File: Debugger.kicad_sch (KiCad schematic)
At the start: 22 parts, among them J1 Header internal clock, J2 I/O, Q1 BC546, SW1 Single step, U1 NE555P, U2 74LS00, U3 74LS74

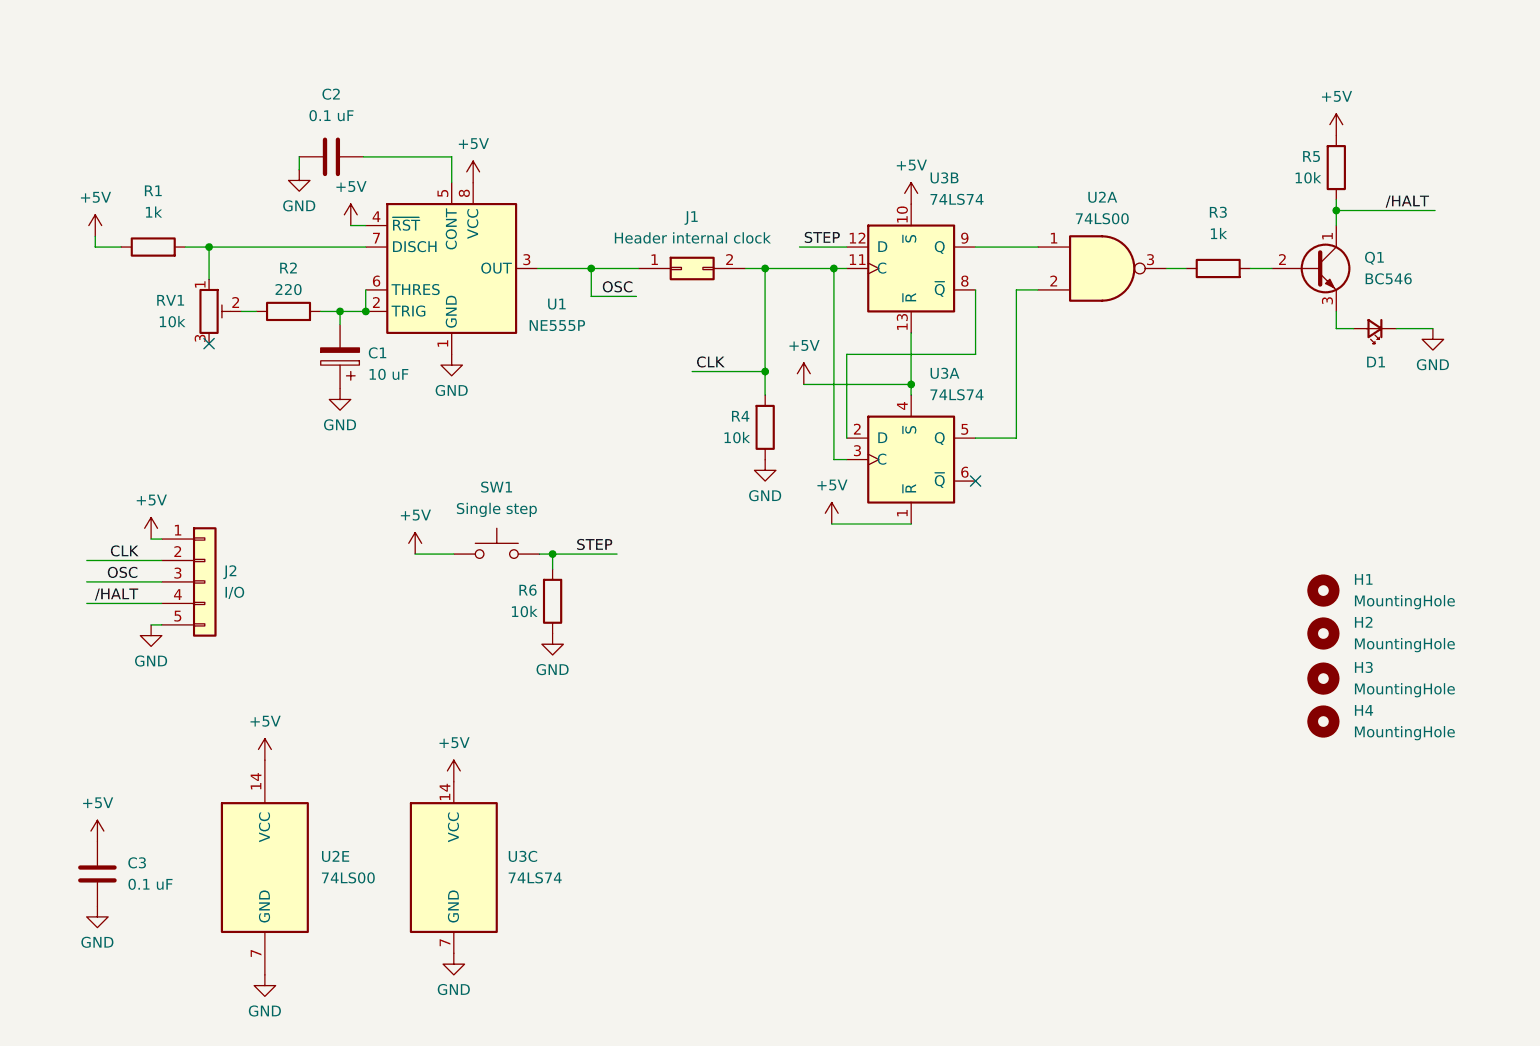
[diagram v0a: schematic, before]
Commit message: Schematic: schmitt trigger, auxilary ports
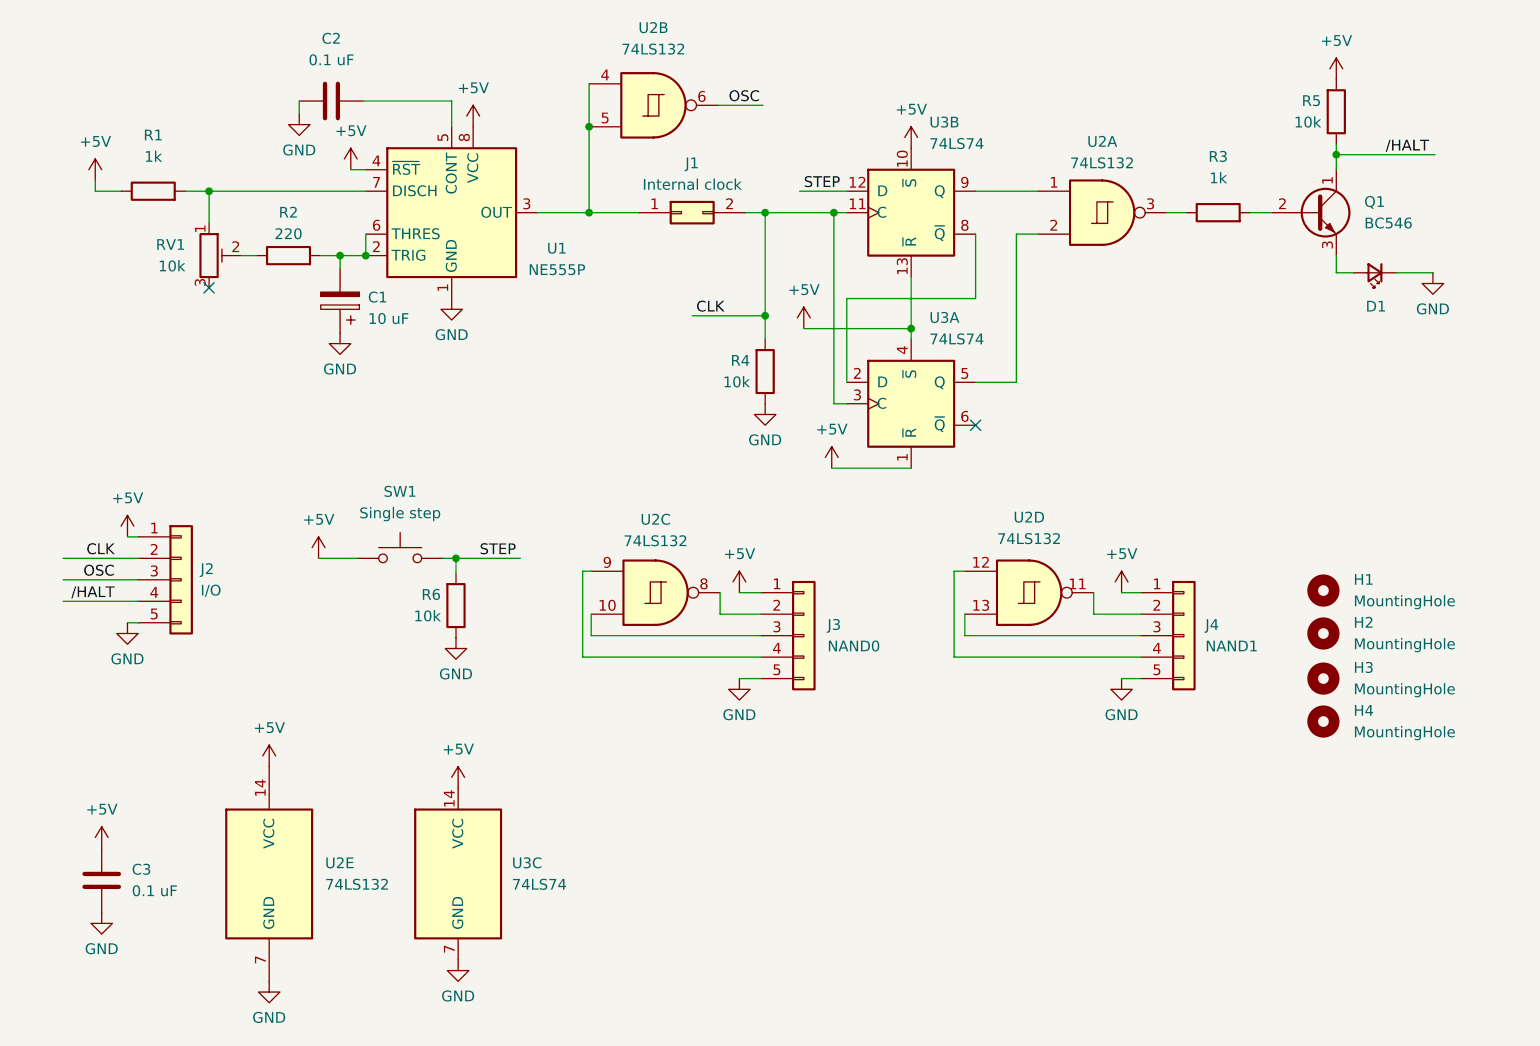
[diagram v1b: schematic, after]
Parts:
- removed U2: 74LS00, Package_DIP:DIP-14_W10.16mm, symbol 74xx:74LS00
- added J3: NAND0, Connector_PinHeader_1.00mm:PinHeader_1x05_P1.00mm_Vertical, symbol Connector_Generic:Conn_01x05
- added J4: NAND1, Connector_PinHeader_1.00mm:PinHeader_1x05_P1.00mm_Vertical, symbol Connector_Generic:Conn_01x05
- added U2: 74LS132, Package_DIP:DIP-14_W7.62mm_Socket, symbol 74xx:74LS132
- added unit 2 of U3
- added unit 3 of U3
- J1: value Header internal clock -> Internal clock
- U1: footprint Package_DIP:DIP-8_W7.62mm -> Package_DIP:DIP-8_W7.62mm_Socket
- U3: footprint Package_DIP:DIP-14_W10.16mm -> Package_DIP:DIP-14_W7.62mm_Socket
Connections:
- net +5V: now also J3.1 (Pin_1), J4.1 (Pin_1), U2.14 (VCC), U3.10 (~{S}), U3.13 (~{R}), U3.14 (VCC); no longer U3.10 (~{S}), U3.13 (~{R}), U3.14 (VCC)
- net CLK: now also U3.11 (C); no longer U3.11 (C)
- net GND: now also J3.5 (Pin_5), J4.5 (Pin_5), U2.7 (GND), U3.7 (GND); no longer U3.7 (GND)
- net OSC: now also U2.6; no longer J1.1 (Pin_1), U1.3 (OUT)
- net STEP: now also U3.12 (D); no longer U3.12 (D)
- net at U3.2 (D): now also U3.8 (~{Q}); no longer U3.8 (~{Q})
- net at U3.5 (Q): now also U2.2
- net at R3.1: now also U2.3
- new net: U2.1, U3.9 (Q)
- new net: J3.3 (Pin_3), U2.10
- new net: J4.2 (Pin_2), U2.11
- new net: J4.4 (Pin_4), U2.12
- new net: J4.3 (Pin_3), U2.13
- new net: J1.1 (Pin_1), U1.3 (OUT), U2.4, U2.5
- new net: J3.2 (Pin_2), U2.8
- new net: J3.4 (Pin_4), U2.9
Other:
- moved on the sheet: C1, C2, C3, D1, J1, J2, Q1, R1, R2, R3, R4, R5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

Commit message: Schematic: fix power flag
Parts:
- added unit 3 of U2
- added unit 5 of U2
- added unit 4 of U2
- added unit 1 of U2
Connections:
- net +5V: now also U2.14 (VCC); no longer U2.14 (VCC)
- net GND: now also U2.7 (GND); no longer U2.7 (GND)
- net at U3.9 (Q): now also U2.1; no longer U2.1
- net at J3.3 (Pin_3): now also U2.10; no longer U2.10
- net at J4.2 (Pin_2): now also U2.11; no longer U2.11
- net at J4.4 (Pin_4): now also U2.12; no longer U2.12
- net at J4.3 (Pin_3): now also U2.13; no longer U2.13
- net at U3.5 (Q): now also U2.2; no longer U2.2
- net at R3.1: now also U2.3; no longer U2.3
- net at J3.2 (Pin_2): now also U2.8; no longer U2.8
- net at J3.4 (Pin_4): now also U2.9; no longer U2.9
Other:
- moved on the sheet: J2
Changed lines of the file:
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@@
 	)
 	(junction
+		(at 34.544 85.852)
+		(diameter 0)
+		(color 0 0 0 0)
+	)
+	(junction
+		(at 34.544 75.692)
+		(diameter 0)
+		(color 0 0 0 0)
+	)
+	(junction
 		(at 82.55 27.178)
 		(diameter 0)
@@
 	(wire
 		(pts
-			(xy 27.94 75.692) (xy 29.21 75.692)
+			(xy 34.544 75.692) (xy 35.814 75.692)
 		)
 		(stroke
@@
 	(wire
 		(pts
+			(xy 29.972 85.852) (xy 34.544 85.852)
+		)
+		(stroke
+			(width 0)
+			(type default)
+		)
+	)
+	(wire
+		(pts
 			(xy 125.73 89.916) (xy 147.828 89.916)
 		)
@@
 	(wire
 		(pts
+			(xy 29.972 75.692) (xy 34.544 75.692)
+		)
+		(stroke
+			(width 0)
+			(type default)
+		)
+	)
+	(wire
+		(pts
 			(xy 133.096 39.878) (xy 135.636 39.878)
 		)
@@
 	(wire
 		(pts
-			(xy 20.32 78.232) (xy 29.21 78.232)
+			(xy 26.924 78.232) (xy 35.814 78.232)
 		)
 		(stroke
@@
 	(wire
 		(pts
-			(xy 20.32 80.772) (xy 29.21 80.772)
+			(xy 26.924 80.772) (xy 35.814 80.772)
 		)
 		(stroke
@@
 	(wire
 		(pts
-			(xy 27.94 85.852) (xy 29.21 85.852)
+			(xy 34.544 85.852) (xy 35.814 85.852)
 		)
 		(stroke
@@
 	(wire
 		(pts
-			(xy 20.32 83.312) (xy 29.21 83.312)
+			(xy 26.924 83.312) (xy 35.814 83.312)
 		)
 		(stroke
@@
 	)
 	(label "OSC"
-		(at 26.416 80.772 180)
+		(at 33.02 80.772 180)
 		(effects
 			(font
@@
 	)
 	(label "{slash}HALT"
-		(at 26.416 83.312 180)
+		(at 33.02 83.312 180)
 		(effects
 			(font
@@
 	)
 	(label "CLK"
-		(at 26.416 78.232 180)
+		(at 33.02 78.232 180)
 		(effects
 			(font
@@
 	(symbol
 		(lib_id "power:GND")
-		(at 27.94 85.852 0)
+		(at 34.544 85.852 0)
 		(unit 1)
 		(body_style 1)
@@
 		(fields_autoplaced yes)
 		(property "Reference" "#PWR021"
-			(at 27.94 92.202 0)
+			(at 34.544 92.202 0)
 			(hide yes)
 			(show_name no)
@@
 		)
 		(property "Value" "GND"
-			(at 27.94 90.17 0)
+			(at 34.544 90.17 0)
 			(show_name no)
 			(do_not_autoplace no)
@@
 		)
 		(property "Footprint" ""
-			(at 27.94 85.852 0)
+			(at 34.544 85.852 0)
 			(hide yes)
 			(show_name no)
@@
 		)
 		(property "Datasheet" ""
-			(at 27.94 85.852 0)
+			(at 34.544 85.852 0)
 			(hide yes)
 			(show_name no)
@@
 		)
 		(property "Description" "Power symbol creates a global label with name \"GND\" , ground"
-			(at 27.94 85.852 0)
+			(at 34.544 85.852 0)
 			(hide yes)
 			(show_name no)
@@
 	(symbol
 		(lib_id "Connector_Generic:Conn_01x05")
-		(at 34.29 80.772 0)
+		(at 40.894 80.772 0)
 		(unit 1)
 		(body_style 1)
@@
 		(fields_autoplaced yes)
 		(property "Reference" "J2"
-			(at 36.576 79.5019 0)
+			(at 43.18 79.5019 0)
 			(show_name no)
 			(do_not_autoplace no)
@@
 		)
 		(property "Value" "I/O"
-			(at 36.576 82.0419 0)
+			(at 43.18 82.0419 0)
 			(show_name no)
 			(do_not_autoplace no)
@@
 		)
 		(property "Footprint" "Connector_PinHeader_1.00mm:PinHeader_1x05_P1.00mm_Vertical"
-			(at 34.29 80.772 0)
+			(at 40.894 80.772 0)
 			(hide yes)
 			(show_name no)
@@
 		)
 		(property "Datasheet" ""
-			(at 34.29 80.772 0)
+			(at 40.894 80.772 0)
 			(hide yes)
 			(show_name no)
@@
 		)
 		(property "Description" "Generic connector, single row, 01x05, script generated (kicad-library-utils/schlib/autogen/connector/)"
-			(at 34.29 80.772 0)
+			(at 40.894 80.772 0)
 			(hide yes)
 			(show_name no)
@@
 	(symbol
 		(lib_id "power:+5V")
-		(at 27.94 75.692 0)
+		(at 34.544 75.692 0)
 		(unit 1)
 		(body_style 1)
@@
 		(fields_autoplaced yes)
 		(property "Reference" "#PWR020"
-			(at 27.94 79.502 0)
+			(at 34.544 79.502 0)
 			(hide yes)
 			(show_name no)
@@
 		)
 		(property "Value" "+5V"
-			(at 27.94 71.12 0)
+			(at 34.544 71.12 0)
 			(show_name no)
 			(do_not_autoplace no)
@@
 		)
 		(property "Footprint" ""
-			(at 27.94 75.692 0)
+			(at 34.544 75.692 0)
 			(hide yes)
 			(show_name no)
@@
 		)
 		(property "Datasheet" ""
-			(at 27.94 75.692 0)
+			(at 34.544 75.692 0)
 			(hide yes)
 			(show_name no)
@@
 		)
 		(property "Description" "Power symbol creates a global label with name \"+5V\""
-			(at 27.94 75.692 0)
+			(at 34.544 75.692 0)
 			(hide yes)
 			(show_name no)
@@
 	)
 	(symbol
+		(lib_id "power:PWR_FLAG")
+		(at 29.972 85.852 90)
+		(unit 1)
+		(body_style 1)
+		(exclude_from_sim no)
+		(in_bom yes)
+		(on_board yes)
+		(in_pos_files yes)
+		(dnp no)
+		(fields_autoplaced yes)
+		(property "Reference" "#FLG01"
+			(at 28.067 85.852 0)
+			(hide yes)
+			(show_name no)
+			(do_not_autoplace no)
+			(effects
+				(font
+					(size 1.27 1.27)
+				)
+			)
+		)
+		(property "Value" "PWR_FLAG"
+			(at 26.162 85.8519 90)
+			(show_name no)
+			(do_not_autoplace no)
+			(effects
+				(font
+					(size 1.27 1.27)
+				)
+				(justify left)
+			)
+		)
+		(property "Footprint" ""
+			(at 29.972 85.852 0)
+			(hide yes)
+			(show_name no)
+			(do_not_autoplace no)
+			(effects
+				(font
+					(size 1.27 1.27)
+				)
+			)
+		)
+		(property "Datasheet" ""
+			(at 29.972 85.852 0)
+			(hide yes)
+			(show_name no)
+			(do_not_autoplace no)
+			(effects
+				(font
+					(size 1.27 1.27)
+				)
+			)
+		)
+		(property "Description" "Special symbol for telling ERC where power comes from"
+			(at 29.972 85.852 0)
+			(hide yes)
+			(show_name no)
+			(do_not_autoplace no)
+			(effects
+				(font
+					(size 1.27 1.27)
+				)
+			)
+		)
+		(pin "1"
+		)
+		(instances
+			(project "Debugger"
+				(path "/a8de7697-6937-4325-b328-e8937268e3c6"
+					(reference "#FLG01")
+					(unit 1)
+				)
+			)
+		)
+	)
+	(symbol
 		(lib_id "Transistor_BJT:BC546")
 		(at 168.402 37.338 0)
@@
 					(unit 1)
 				)
+			)
+		)
+	)
+	(symbol
+		(lib_id "power:PWR_FLAG")
+		(at 29.972 75.692 90)
+		(unit 1)
+		(body_style 1)
+		(exclude_from_sim no)
+		(in_bom yes)
+		(on_board yes)
+		(in_pos_files yes)
+		(dnp no)
+		(fields_autoplaced yes)
+		(property "Reference" "#FLG02"
+			(at 28.067 75.692 0)
+			(hide yes)
+			(show_name no)
+			(do_not_autoplace no)
+			(effects
+				(font
+					(size 1.27 1.27)
+				)
+			)
+		)
+		(property "Value" "PWR_FLAG"
+			(at 26.162 75.6919 90)
+			(show_name no)
+			(do_not_autoplace no)
+			(effects
+				(font
+					(size 1.27 1.27)
+				)
+				(justify left)
+			)
+		)
+		(property "Footprint" ""
+			(at 29.972 75.692 0)
+			(hide yes)
+			(show_name no)
+			(do_not_autoplace no)
+			(effects
+				(font
+					(size 1.27 1.27)
+				)
+			)
+		)
+		(property "Datasheet" ""
+			(at 29.972 75.692 0)
+			(hide yes)
+			(show_name no)
+			(do_not_autoplace no)
+			(effects
+				(font
+					(size 1.27 1.27)
+				)
+			)
+		)
+		(property "Description" "Special symbol for telling ERC where power comes from"
+			(at 29.972 75.692 0)
+			(hide yes)
+			(show_name no)
+			(do_not_autoplace no)
+			(effects
+				(font
+					(size 1.27 1.27)
+				)
+			)
+		)
+		(pin "1"
+		)
+		(instances
+			(project "Debugger"
+				(path "/a8de7697-6937-4325-b328-e8937268e3c6"
+					(reference "#FLG02")
+					(unit 1)
+				)
